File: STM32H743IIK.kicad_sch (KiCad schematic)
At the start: 34 parts, among them U1 STM32H743IIKx, Y1 25MHz, Y2 32.768KHz

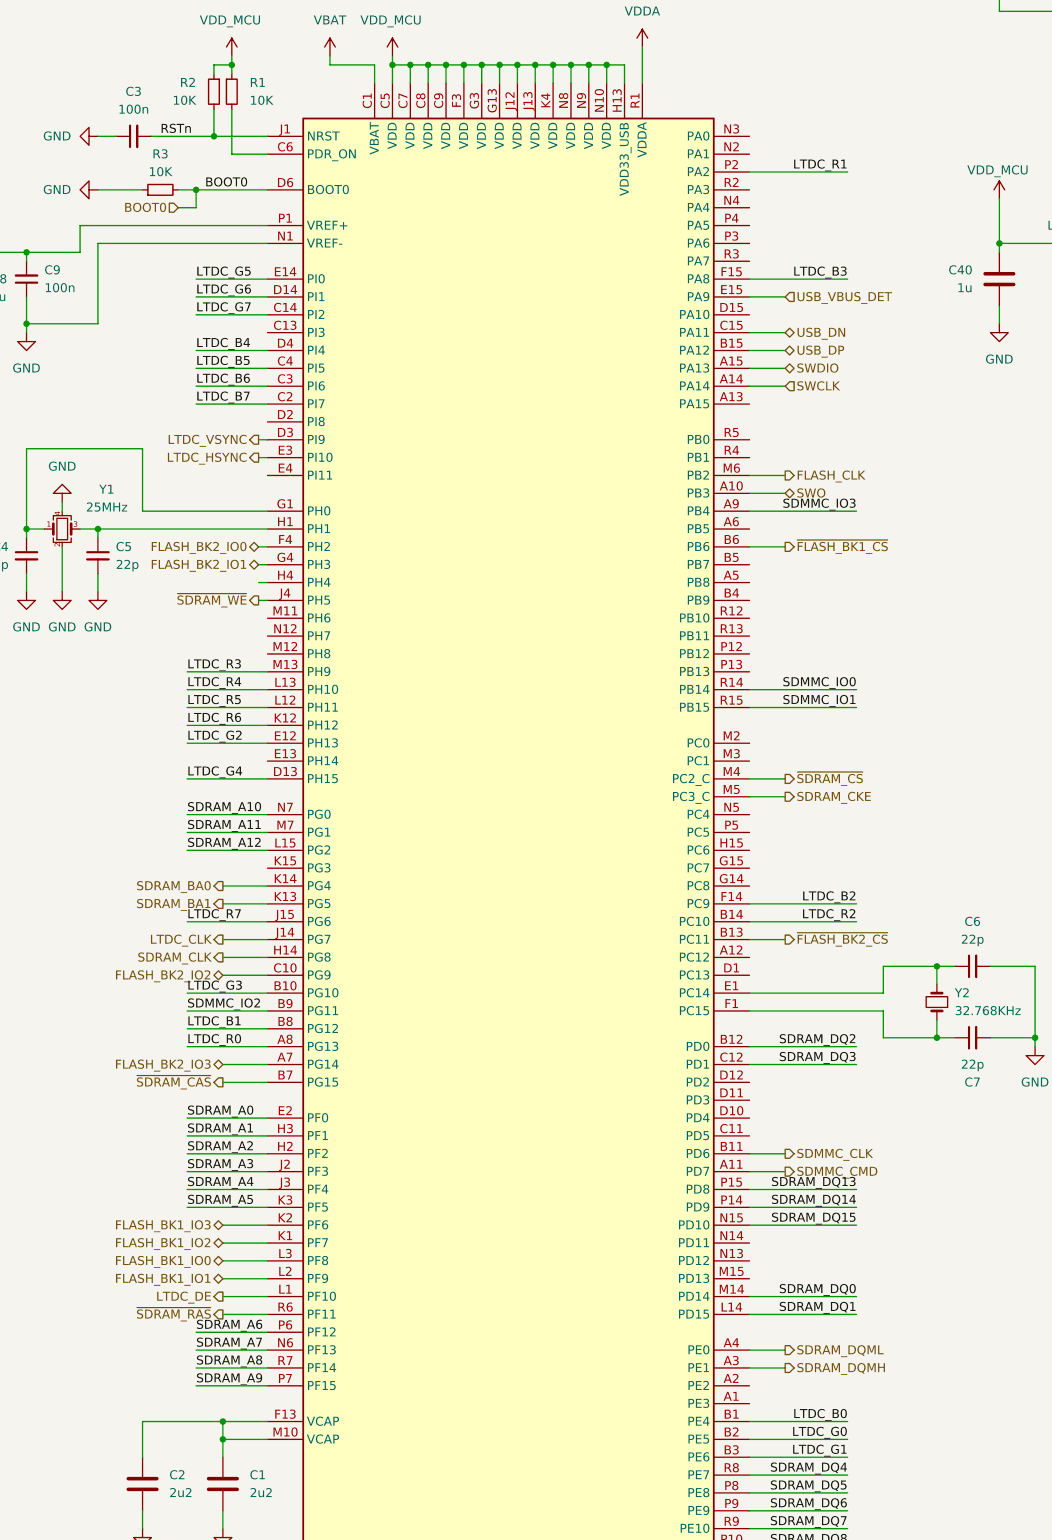
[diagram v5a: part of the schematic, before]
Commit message: Finished fanout all remaining pin, Power block left
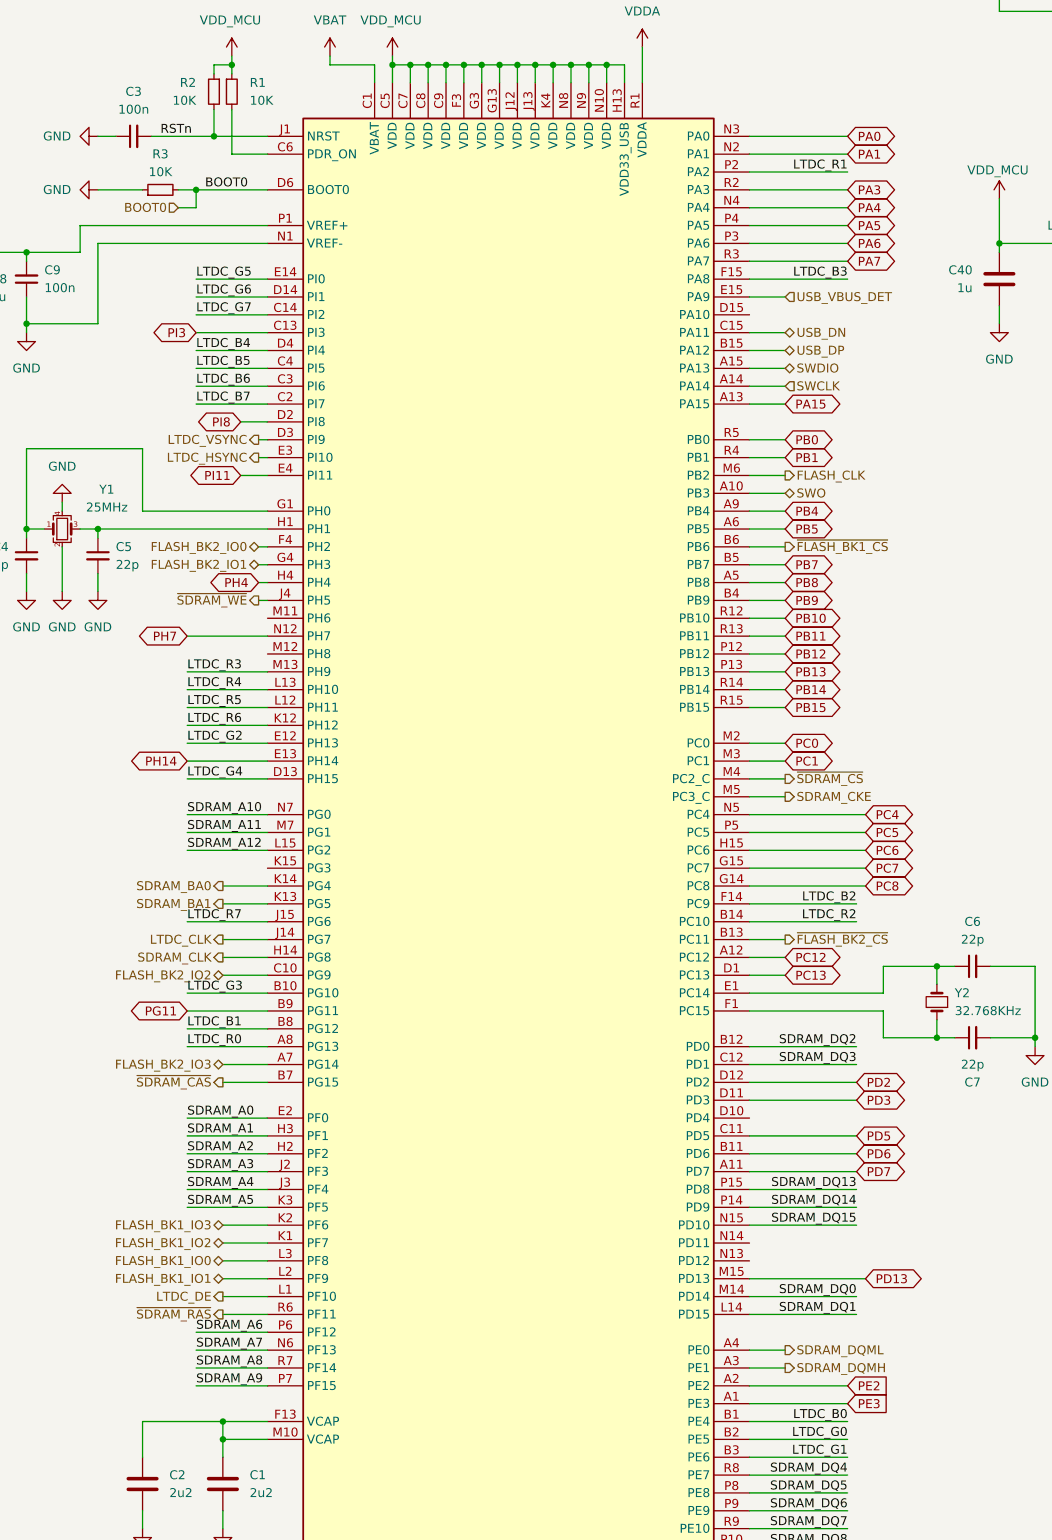
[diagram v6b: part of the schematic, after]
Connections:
- net SDMMC_CLK: no longer U1.B11 (PD6)
- net SDMMC_CMD: no longer U1.A11 (PD7)
- net PE3: now reaches U1.A1 (PE3)
- net PC12: now reaches U1.A12 (PC12)
- net PA15: now reaches U1.A13 (PA15)
- net PE2: now reaches U1.A2 (PE2)
- net PB8: now reaches U1.A5 (PB8)
- net PB5: now reaches U1.A6 (PB5)
- net PB9: now reaches U1.B4 (PB9)
- net PB7: now reaches U1.B5 (PB7)
- net PD5: now reaches U1.C11 (PD5)
- net PI3: now reaches U1.C13 (PI3)
- net PC13: now reaches U1.D1 (PC13)
- net PD3: now reaches U1.D11 (PD3)
- net PD2: now reaches U1.D12 (PD2)
- net PI8: now reaches U1.D2 (PI8)
- net PH14: now reaches U1.E13 (PH14)
- net PI11: now reaches U1.E4 (PI11)
- net PC8: now reaches U1.G14 (PC8)
- net PC7: now reaches U1.G15 (PC7)
- net PC6: now reaches U1.H15 (PC6)
- net PH4: now reaches U1.H4 (PH4)
- net PD13: now reaches U1.M15 (PD13)
- net PC0: now reaches U1.M2 (PC0)
- net PC1: now reaches U1.M3 (PC1)
- net PH7: now reaches U1.N12 (PH7)
- net PA1: now reaches U1.N2 (PA1)
- net PA0: now reaches U1.N3 (PA0)
- net PA4: now reaches U1.N4 (PA4)
- net PC4: now reaches U1.N5 (PC4)
- net PB12: now reaches U1.P12 (PB12)
- net PB13: now reaches U1.P13 (PB13)
- net PA6: now reaches U1.P3 (PA6)
- net PA5: now reaches U1.P4 (PA5)
- net PC5: now reaches U1.P5 (PC5)
- net PB10: now reaches U1.R12 (PB10)
- net PB11: now reaches U1.R13 (PB11)
- net PA3: now reaches U1.R2 (PA3)
- net PA7: now reaches U1.R3 (PA7)
- net PB1: now reaches U1.R4 (PB1)
- net PB0: now reaches U1.R5 (PB0)
- net SDMMC_IO0 renamed PB14
- net SDMMC_IO1 renamed PB15
- net SDMMC_IO2 renamed PG11
- net SDMMC_IO3 renamed PB4
- new net PD6: U1.B11 (PD6)
- new net PD7: U1.A11 (PD7)

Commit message: generate doc
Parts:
- added D1: BAT54CW, Package_TO_SOT_SMD:SOT-23, symbol Diode:BAT54CW
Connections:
- net +3V3: now also D1.1
- net VBAT: now also D1.3
- net RSTn renamed NRST
- new net VRTC: D1.2
